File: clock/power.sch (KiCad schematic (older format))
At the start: 50 parts, among them Q501 BSS138, Q502 BSS138, U501 TPS56428, U502 TPS56428, U503 TPS56428

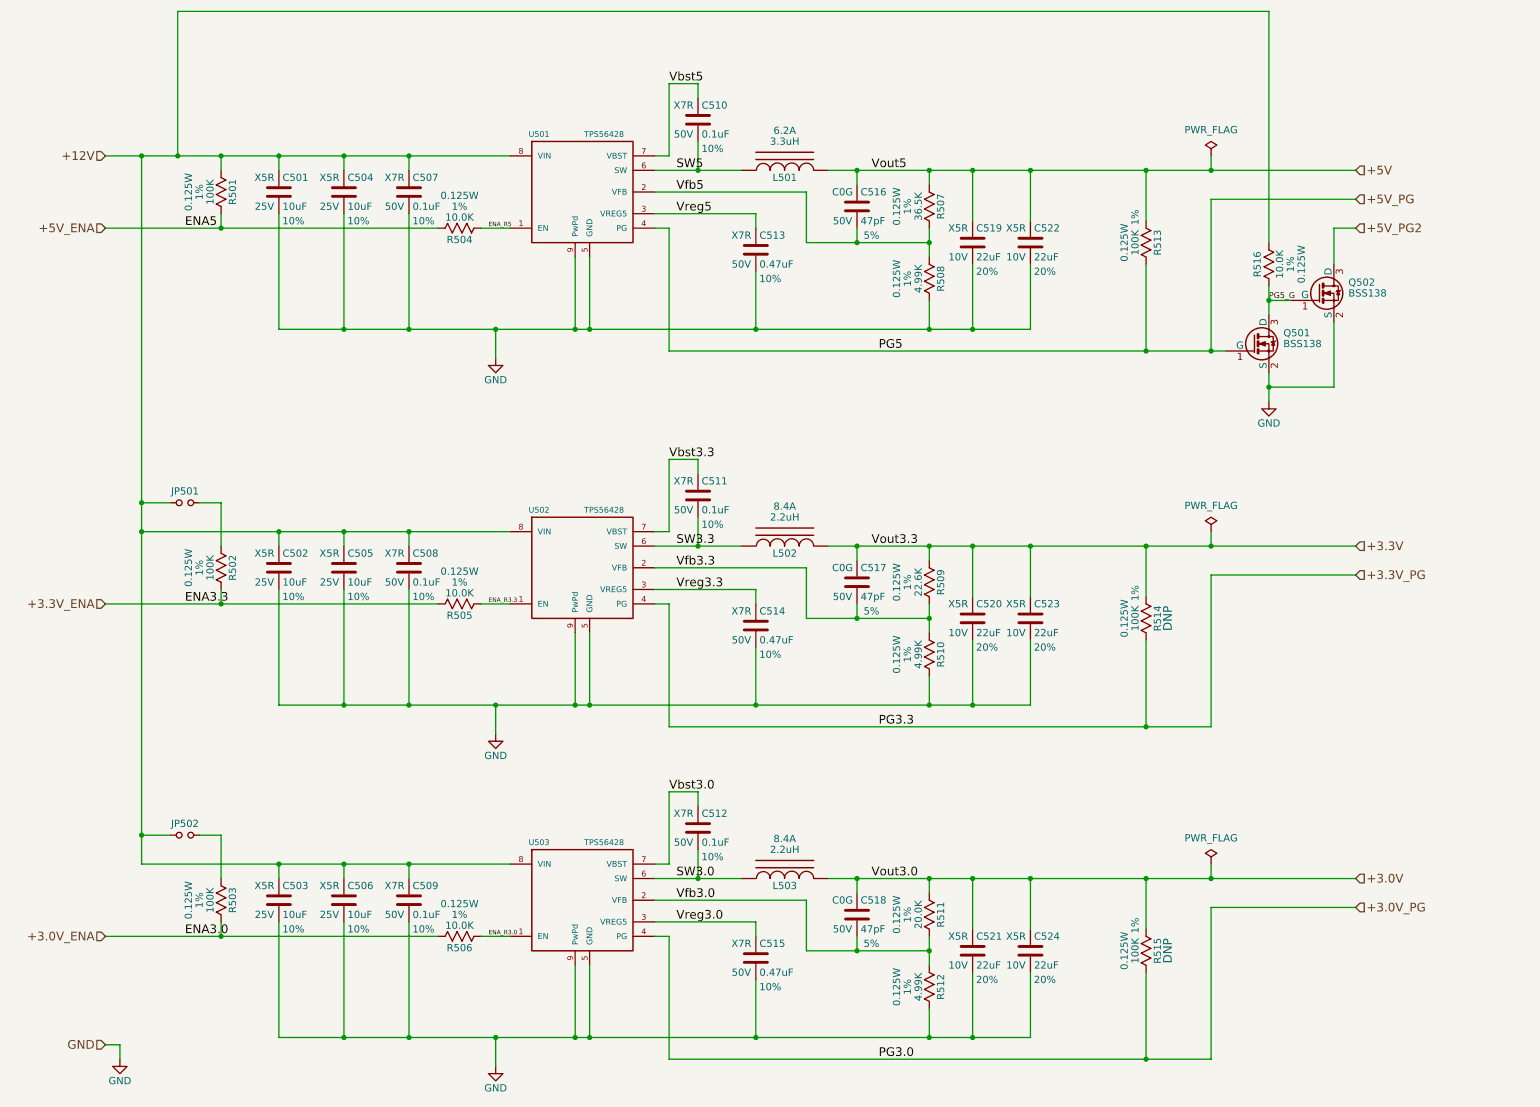
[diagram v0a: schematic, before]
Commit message: Start next revision of the main board. Power sequencing and control changes.
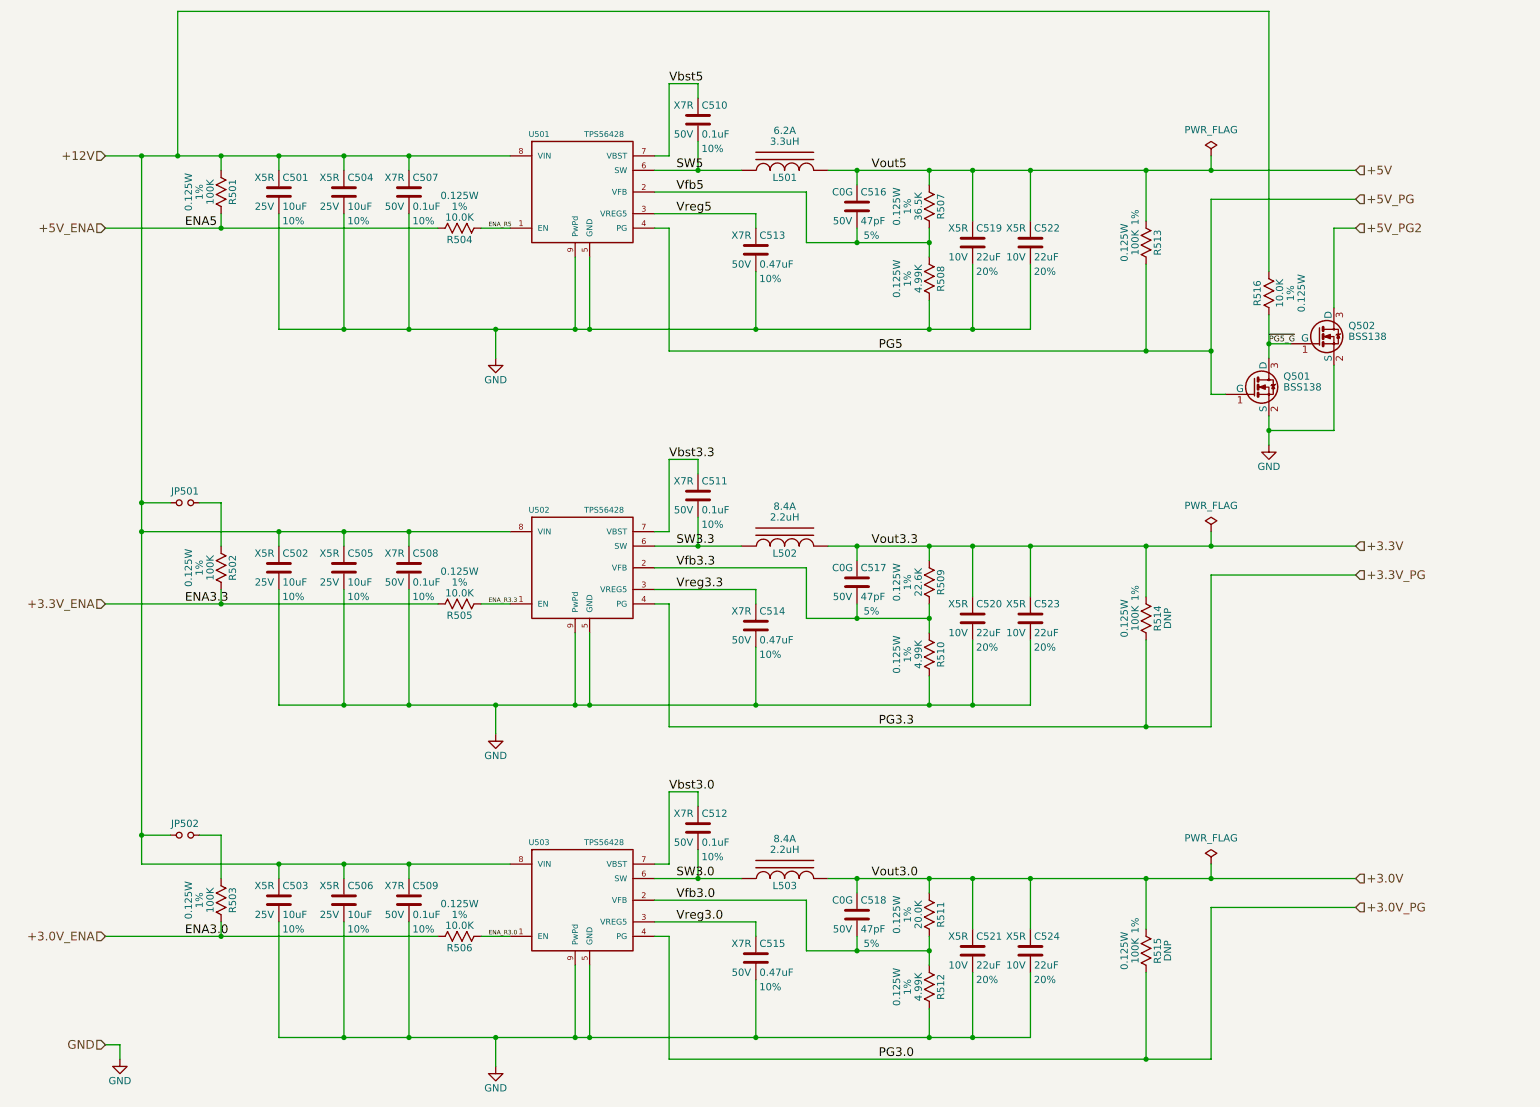
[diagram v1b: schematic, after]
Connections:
- net PG5_G renamed ~PG5_G~
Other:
- moved on the sheet: Q501, Q502, R516
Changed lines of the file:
@@
 	3500 2750 5800 2750
 Wire Wire Line
-	7400 3600 11250 3600
+	7400 3600 11150 3600
+Wire Wire Line
+	11150 2550 11150 3900
+Wire Wire Line
+	11150 3900 11250 3900
 Wire Wire Line
 	6850 3450 6850 2950
@@
 Connection ~ 4300 2750
 $Comp
-L GND #PWR072
+L GND #PWR075
 U 1 1 55FF67B4
 P 6200 3650
-F 0 "#PWR072" H 6200 3400 50  0001 C CNN
+F 0 "#PWR075" H 6200 3400 50  0001 C CNN
 F 1 "GND" H 6200 3500 50  0000 C CNN
 F 2 "" H 6200 3650 60  0000 C CNN
@@
 Connection ~ 4300 5350
 $Comp
-L GND #PWR073
+L GND #PWR076
 U 1 1 5619E4B9
 P 6200 6250
-F 0 "#PWR073" H 6200 6000 50  0001 C CNN
+F 0 "#PWR076" H 6200 6000 50  0001 C CNN
 F 1 "GND" H 6200 6100 50  0000 C CNN
 F 2 "" H 6200 6250 60  0000 C CNN
@@
 Connection ~ 4300 7650
 $Comp
-L GND #PWR074
+L GND #PWR077
 U 1 1 561A0FCA
 P 6200 8550
-F 0 "#PWR074" H 6200 8300 50  0001 C CNN
+F 0 "#PWR077" H 6200 8300 50  0001 C CNN
 F 1 "GND" H 6200 8400 50  0000 C CNN
 F 2 "" H 6200 8550 60  0000 C CNN
@@
 	12150 2550 11150 2550
 Wire Wire Line
-	11150 2550 11150 3600
-Wire Wire Line
 	12150 5150 11150 5150
 Wire Wire Line
@@
 F 6 "Vishay Dale" V 10700 5450 50  0001 C CNN "Manufacturer"
 F 7 "CRCW0805100KFKEA" V 10850 5450 50  0001 C CNN "PartNum"
-F 8 "DNP" V 10850 5450 60  0000 C CNN "DNP"
+F 8 "DNP" V 10850 5450 50  0000 C CNN "DNP"
 	1    10700 5450
 	1    0    0    -1
@@
 F 6 "Vishay Dale" V 10700 7750 50  0001 C CNN "Manufacturer"
 F 7 "CRCW0805100KFKEA" V 10850 7750 50  0001 C CNN "PartNum"
-F 8 "DNP" V 10850 7750 60  0000 C CNN "DNP"
+F 8 "DNP" V 10850 7750 50  0000 C CNN "DNP"
 	1    10700 7750
 	1    0    0    -1
@@
 GND
 $Comp
-L GND #PWR075
+L GND #PWR078
 U 1 1 563D8E93
 P 3600 8500
-F 0 "#PWR075" H 3600 8250 50  0001 C CNN
+F 0 "#PWR078" H 3600 8250 50  0001 C CNN
 F 1 "GND" H 3600 8350 50  0000 C CNN
 F 2 "" H 3600 8500 60  0000 C CNN
@@
 	3600 8400 3500 8400
 $Comp
-L PWR_FLAG #FLG076
+L PWR_FLAG #FLG079
 U 1 1 56439BF3
 P 11150 2250
-F 0 "#FLG076" H 11150 2345 50  0001 C CNN
+F 0 "#FLG079" H 11150 2345 50  0001 C CNN
 F 1 "PWR_FLAG" H 11150 2430 50  0000 C CNN
 F 2 "" H 11150 2250 60  0000 C CNN
@@
 Connection ~ 11150 2350
 $Comp
-L PWR_FLAG #FLG077
+L PWR_FLAG #FLG080
 U 1 1 5643A4B3
 P 11150 4850
-F 0 "#FLG077" H 11150 4945 50  0001 C CNN
+F 0 "#FLG080" H 11150 4945 50  0001 C CNN
 F 1 "PWR_FLAG" H 11150 5030 50  0000 C CNN
 F 2 "" H 11150 4850 60  0000 C CNN
@@
 Connection ~ 11150 4950
 $Comp
-L PWR_FLAG #FLG078
+L PWR_FLAG #FLG081
 U 1 1 5643AC28
 P 11150 7150
-F 0 "#FLG078" H 11150 7245 50  0001 C CNN
+F 0 "#FLG081" H 11150 7245 50  0001 C CNN
 F 1 "PWR_FLAG" H 11150 7330 50  0000 C CNN
 F 2 "" H 11150 7150 60  0000 C CNN
@@
 L BSS138 Q501
 U 1 1 57A96588
-P 11450 3550
-F 0 "Q501" H 11650 3625 50  0000 L CNN
-F 1 "BSS138" H 11650 3550 50  0000 L CNN
-F 2 "local:SOT-23-3_NXP_HandSoldering" H 11650 3475 50  0001 L CIN
-F 3 "" H 11450 3550 50  0000 L CNN
-F 4 "ON Semiconductor" H 11450 3550 60  0001 C CNN "Manufacturer"
-F 5 "BSS138LT1G" H 11450 3550 60  0001 C CNN "PartNum"
-	1    11450 3550
+P 11450 3850
+F 0 "Q501" H 11650 3925 50  0000 L CNN
+F 1 "BSS138" H 11650 3850 50  0000 L CNN
+F 2 "local:SOT-23-3_NXP_HandSoldering" H 11650 3775 50  0001 L CIN
+F 3 "" H 11450 3850 50  0000 L CNN
+F 4 "ON Semiconductor" H 11450 3850 60  0001 C CNN "Manufacturer"
+F 5 "BSS138LT1G" H 11450 3850 60  0001 C CNN "PartNum"
+	1    11450 3850
 	1    0    0    -1
 $EndComp
@@
 L BSS138 Q502
 U 1 1 57A97046
-P 11900 3200
-F 0 "Q502" H 12100 3275 50  0000 L CNN
-F 1 "BSS138" H 12100 3200 50  0000 L CNN
-F 2 "local:SOT-23-3_NXP_HandSoldering" H 12100 3125 50  0001 L CIN
-F 3 "" H 11900 3200 50  0000 L CNN
-F 4 "ON Semiconductor" H 11900 3200 60  0001 C CNN "Manufacturer"
-F 5 "BSS138LT1G" H 11900 3200 60  0001 C CNN "PartNum"
-	1    11900 3200
+P 11900 3500
+F 0 "Q502" H 12100 3575 50  0000 L CNN
+F 1 "BSS138" H 12100 3500 50  0000 L CNN
+F 2 "local:SOT-23-3_NXP_HandSoldering" H 12100 3425 50  0001 L CIN
+F 3 "" H 11900 3500 50  0000 L CNN
+F 4 "ON Semiconductor" H 11900 3500 60  0001 C CNN "Manufacturer"
+F 5 "BSS138LT1G" H 11900 3500 60  0001 C CNN "PartNum"
+	1    11900 3500
 	1    0    0    -1
 $EndComp
@@
 L R_local R516
 U 1 1 57A9749D
-P 11550 3000
-F 0 "R516" V 11630 3000 50  0000 C CNN
-F 1 "10.0K" V 11475 3000 50  0000 C CNN
-F 2 "Resistors_SMD:R_0805_HandSoldering" V 11480 3000 30  0001 C CNN
-F 3 "" V 11630 3000 30  0000 C CNN
-F 4 "1%" V 11400 3000 50  0000 C CNN "Tolerance"
-F 5 "0.125W" V 11325 3000 50  0000 C CNN "Power"
-F 6 "Vishay Dale" V 11550 3000 50  0001 C CNN "Manufacturer"
-F 7 "CRCW080510K0FKEA" V 11700 3000 50  0001 C CNN "PartNum"
-	1    11550 3000
+P 11550 3200
+F 0 "R516" V 11630 3200 50  0000 C CNN
+F 1 "10.0K" V 11475 3200 50  0000 C CNN
+F 2 "Resistors_SMD:R_0805_HandSoldering" V 11480 3200 30  0001 C CNN
+F 3 "" V 11630 3200 30  0000 C CNN
+F 4 "1%" V 11400 3200 50  0000 C CNN "Tolerance"
+F 5 "0.125W" V 11325 3200 50  0000 C CNN "Power"
+F 6 "Vishay Dale" V 11550 3200 50  0001 C CNN "Manufacturer"
+F 7 "CRCW080510K0FKEA" V 11700 3200 50  0001 C CNN "PartNum"
+	1    11550 3200
 	-1   0    0    1
 $EndComp
 Wire Wire Line
-	11550 3150 11550 3350
-Wire Wire Line
-	11700 3250 11550 3250
-Connection ~ 11550 3250
-Wire Wire Line
-	12000 3400 12000 3850
-Wire Wire Line
-	12000 3850 11550 3850
-Wire Wire Line
-	11550 3750 11550 3950
-$Comp
-L GND #PWR079
+	11550 3350 11550 3650
+Wire Wire Line
+	11700 3550 11550 3550
+Connection ~ 11550 3550
+Wire Wire Line
+	12000 3700 12000 4150
+Wire Wire Line
+	12000 4150 11550 4150
+Wire Wire Line
+	11550 4050 11550 4250
+$Comp
+L GND #PWR082
 U 1 1 57A97EAC
-P 11550 3950
-F 0 "#PWR079" H 11550 3700 50  0001 C CNN
-F 1 "GND" H 11550 3800 50  0000 C CNN
-F 2 "" H 11550 3950 60  0000 C CNN
-F 3 "" H 11550 3950 60  0000 C CNN
-	1    11550 3950
-	1    0    0    -1
-$EndComp
-Connection ~ 11550 3850
+P 11550 4250
+F 0 "#PWR082" H 11550 4000 50  0001 C CNN
+F 1 "GND" H 11550 4100 50  0000 C CNN
+F 2 "" H 11550 4250 60  0000 C CNN
+F 3 "" H 11550 4250 60  0000 C CNN
+	1    11550 4250
+	1    0    0    -1
+$EndComp
+Connection ~ 11550 4150
 Connection ~ 11150 3600
 Wire Wire Line
-	12000 3000 12000 2750
+	12000 3300 12000 2750
 Wire Wire Line
 	12000 2750 12150 2750
 Wire Wire Line
-	11550 2850 11550 1250
+	11550 3050 11550 1250
 Wire Wire Line
 	11550 1250 4000 1250
@@
 	4000 1250 4000 2250
 Connection ~ 4000 2250
-Text Label 11550 3250 0    40   ~ 0
-PG5_G
+Text Label 11550 3550 0    40   ~ 0
+~PG5_G~
 $EndSCHEMATC

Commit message: Checkpoint layout. Update hand soldering footprints for 0805 parts.
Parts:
- C507, C508, C509, C510, C511, C512, C513, C514, C515, C516, C517, C518: footprint Capacitors_SMD:C_0805_HandSoldering -> local:C_0805_HandSoldering
- R501, R502, R503, R504, R505, R506, R507, R508, R509, R510, R511, R512, R513, R514, R515, R516: footprint Resistors_SMD:R_0805_HandSoldering -> local:R_0805_HandSoldering
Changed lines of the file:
@@
 F 0 "C507" H 5625 2600 50  0000 L CNN
 F 1 "0.1uF" H 5625 2400 50  0000 L CNN
-F 2 "Capacitors_SMD:C_0805_HandSoldering" H 5638 2350 30  0001 C CNN
+F 2 "local:C_0805_HandSoldering" H 5638 2350 30  0001 C CNN
 F 3 "" H 5600 2500 60  0000 C CNN
 F 4 "50V" H 5500 2400 50  0000 C CNN "Voltage"
@@
 F 0 "R501" V 4380 2500 50  0000 C CNN
 F 1 "100K" V 4225 2500 50  0000 C CNN
-F 2 "Resistors_SMD:R_0805_HandSoldering" V 4230 2500 30  0001 C CNN
+F 2 "local:R_0805_HandSoldering" V 4230 2500 30  0001 C CNN
 F 3 "" V 4380 2500 30  0000 C CNN
 F 4 "1%" V 4150 2500 50  0000 C CNN "Tolerance"
@@
 F 0 "R504" V 6030 2750 50  0000 C CNN
 F 1 "10.0K" V 5875 2750 50  0000 C CNN
-F 2 "Resistors_SMD:R_0805_HandSoldering" V 5880 2750 30  0001 C CNN
+F 2 "local:R_0805_HandSoldering" V 5880 2750 30  0001 C CNN
 F 3 "" V 6030 2750 30  0000 C CNN
 F 4 "1%" V 5800 2750 50  0000 C CNN "Tolerance"
@@
 F 0 "R513" V 10780 2850 50  0000 C CNN
 F 1 "100K" V 10625 2850 50  0000 C CNN
-F 2 "Resistors_SMD:R_0805_HandSoldering" V 10630 2850 30  0001 C CNN
+F 2 "local:R_0805_HandSoldering" V 10630 2850 30  0001 C CNN
 F 3 "" V 10780 2850 30  0000 C CNN
 F 4 "1%" V 10625 3025 50  0000 C CNN "Tolerance"
@@
 F 0 "C510" H 7625 2100 50  0000 L CNN
 F 1 "0.1uF" H 7625 1900 50  0000 L CNN
-F 2 "Capacitors_SMD:C_0805_HandSoldering" H 7638 1850 30  0001 C CNN
+F 2 "local:C_0805_HandSoldering" H 7638 1850 30  0001 C CNN
 F 3 "" H 7600 2000 60  0000 C CNN
 F 4 "50V" H 7500 1900 50  0000 C CNN "Voltage"
@@
 F 0 "C513" H 8025 3000 50  0000 L CNN
 F 1 "0.47uF" H 8025 2800 50  0000 L CNN
-F 2 "Capacitors_SMD:C_0805_HandSoldering" H 8038 2750 30  0001 C CNN
+F 2 "local:C_0805_HandSoldering" H 8038 2750 30  0001 C CNN
 F 3 "" H 8000 2900 60  0000 C CNN
 F 4 "50V" H 7900 2800 50  0000 C CNN "Voltage"
@@
 F 0 "C508" H 5625 5200 50  0000 L CNN
 F 1 "0.1uF" H 5625 5000 50  0000 L CNN
-F 2 "Capacitors_SMD:C_0805_HandSoldering" H 5638 4950 30  0001 C CNN
+F 2 "local:C_0805_HandSoldering" H 5638 4950 30  0001 C CNN
 F 3 "" H 5600 5100 60  0000 C CNN
 F 4 "50V" H 5500 5000 50  0000 C CNN "Voltage"
@@
 F 0 "R505" V 6030 5350 50  0000 C CNN
 F 1 "10.0K" V 5875 5350 50  0000 C CNN
-F 2 "Resistors_SMD:R_0805_HandSoldering" V 5880 5350 30  0001 C CNN
+F 2 "local:R_0805_HandSoldering" V 5880 5350 30  0001 C CNN
 F 3 "" V 6030 5350 30  0000 C CNN
 F 4 "1%" V 5800 5350 50  0000 C CNN "Tolerance"
@@
 F 0 "R502" V 4380 5100 50  0000 C CNN
 F 1 "100K" V 4225 5100 50  0000 C CNN
-F 2 "Resistors_SMD:R_0805_HandSoldering" V 4230 5100 30  0001 C CNN
+F 2 "local:R_0805_HandSoldering" V 4230 5100 30  0001 C CNN
 F 3 "" V 4380 5100 30  0000 C CNN
 F 4 "1%" V 4150 5100 50  0000 C CNN "Tolerance"
@@
 F 0 "C511" H 7625 4700 50  0000 L CNN
 F 1 "0.1uF" H 7625 4500 50  0000 L CNN
-F 2 "Capacitors_SMD:C_0805_HandSoldering" H 7638 4450 30  0001 C CNN
+F 2 "local:C_0805_HandSoldering" H 7638 4450 30  0001 C CNN
 F 3 "" H 7600 4600 60  0000 C CNN
 F 4 "50V" H 7500 4500 50  0000 C CNN "Voltage"
@@
 F 0 "C514" H 8025 5600 50  0000 L CNN
 F 1 "0.47uF" H 8025 5400 50  0000 L CNN
-F 2 "Capacitors_SMD:C_0805_HandSoldering" H 8038 5350 30  0001 C CNN
+F 2 "local:C_0805_HandSoldering" H 8038 5350 30  0001 C CNN
 F 3 "" H 8000 5500 60  0000 C CNN
 F 4 "50V" H 7900 5400 50  0000 C CNN "Voltage"
@@
 F 0 "R514" V 10780 5450 50  0000 C CNN
 F 1 "100K" V 10625 5450 50  0000 C CNN
-F 2 "Resistors_SMD:R_0805_HandSoldering" V 10630 5450 30  0001 C CNN
+F 2 "local:R_0805_HandSoldering" V 10630 5450 30  0001 C CNN
 F 3 "" V 10780 5450 30  0000 C CNN
 F 4 "1%" V 10625 5625 50  0000 C CNN "Tolerance"
@@
 F 0 "R515" V 10780 7750 50  0000 C CNN
 F 1 "100K" V 10625 7750 50  0000 C CNN
-F 2 "Resistors_SMD:R_0805_HandSoldering" V 10630 7750 30  0001 C CNN
+F 2 "local:R_0805_HandSoldering" V 10630 7750 30  0001 C CNN
 F 3 "" V 10780 7750 30  0000 C CNN
 F 4 "1%" V 10625 7925 50  0000 C CNN "Tolerance"
@@
 F 0 "C515" H 8025 7900 50  0000 L CNN
 F 1 "0.47uF" H 8025 7700 50  0000 L CNN
-F 2 "Capacitors_SMD:C_0805_HandSoldering" H 8038 7650 30  0001 C CNN
+F 2 "local:C_0805_HandSoldering" H 8038 7650 30  0001 C CNN
 F 3 "" H 8000 7800 60  0000 C CNN
 F 4 "50V" H 7900 7700 50  0000 C CNN "Voltage"
@@
 F 0 "C512" H 7625 7000 50  0000 L CNN
 F 1 "0.1uF" H 7625 6800 50  0000 L CNN
-F 2 "Capacitors_SMD:C_0805_HandSoldering" H 7638 6750 30  0001 C CNN
+F 2 "local:C_0805_HandSoldering" H 7638 6750 30  0001 C CNN
 F 3 "" H 7600 6900 60  0000 C CNN
 F 4 "50V" H 7500 6800 50  0000 C CNN "Voltage"
@@
 F 0 "R506" V 6030 7650 50  0000 C CNN
 F 1 "10.0K" V 5875 7650 50  0000 C CNN
-F 2 "Resistors_SMD:R_0805_HandSoldering" V 5880 7650 30  0001 C CNN
+F 2 "local:R_0805_HandSoldering" V 5880 7650 30  0001 C CNN
 F 3 "" V 6030 7650 30  0000 C CNN
 F 4 "1%" V 5800 7650 50  0000 C CNN "Tolerance"
@@
 F 0 "C509" H 5625 7500 50  0000 L CNN
 F 1 "0.1uF" H 5625 7300 50  0000 L CNN
-F 2 "Capacitors_SMD:C_0805_HandSoldering" H 5638 7250 30  0001 C CNN
+F 2 "local:C_0805_HandSoldering" H 5638 7250 30  0001 C CNN
 F 3 "" H 5600 7400 60  0000 C CNN
 F 4 "50V" H 5500 7300 50  0000 C CNN "Voltage"
@@
 F 0 "R503" V 4380 7400 50  0000 C CNN
 F 1 "100K" V 4225 7400 50  0000 C CNN
-F 2 "Resistors_SMD:R_0805_HandSoldering" V 4230 7400 30  0001 C CNN
+F 2 "local:R_0805_HandSoldering" V 4230 7400 30  0001 C CNN
 F 3 "" V 4380 7400 30  0000 C CNN
 F 4 "1%" V 4150 7400 50  0000 C CNN "Tolerance"
@@
 F 0 "R508" V 9280 3100 50  0000 C CNN
 F 1 "4.99K" V 9125 3100 50  0000 C CNN
-F 2 "Resistors_SMD:R_0805_HandSoldering" V 9130 3100 30  0001 C CNN
+F 2 "local:R_0805_HandSoldering" V 9130 3100 30  0001 C CNN
 F 3 "" V 9280 3100 30  0000 C CNN
 F 4 "1%" V 9050 3100 50  0000 C CNN "Tolerance"
@@
 F 0 "R507" V 9280 2600 50  0000 C CNN
 F 1 "36.5K" V 9125 2600 50  0000 C CNN
-F 2 "Resistors_SMD:R_0805_HandSoldering" V 9130 2600 30  0001 C CNN
+F 2 "local:R_0805_HandSoldering" V 9130 2600 30  0001 C CNN
 F 3 "" V 9280 2600 30  0000 C CNN
 F 4 "1%" V 9050 2600 50  0000 C CNN "Tolerance"
@@
 F 0 "R510" V 9280 5700 50  0000 C CNN
 F 1 "4.99K" V 9125 5700 50  0000 C CNN
-F 2 "Resistors_SMD:R_0805_HandSoldering" V 9130 5700 30  0001 C CNN
+F 2 "local:R_0805_HandSoldering" V 9130 5700 30  0001 C CNN
 F 3 "" V 9280 5700 30  0000 C CNN
 F 4 "1%" V 9050 5700 50  0000 C CNN "Tolerance"
@@
 F 0 "R512" V 9280 8000 50  0000 C CNN
 F 1 "4.99K" V 9125 8000 50  0000 C CNN
-F 2 "Resistors_SMD:R_0805_HandSoldering" V 9130 8000 30  0001 C CNN
+F 2 "local:R_0805_HandSoldering" V 9130 8000 30  0001 C CNN
 F 3 "" V 9280 8000 30  0000 C CNN
 F 4 "1%" V 9050 8000 50  0000 C CNN "Tolerance"
@@
 F 0 "R509" V 9280 5200 50  0000 C CNN
 F 1 "22.6K" V 9125 5200 50  0000 C CNN
-F 2 "Resistors_SMD:R_0805_HandSoldering" V 9130 5200 30  0001 C CNN
+F 2 "local:R_0805_HandSoldering" V 9130 5200 30  0001 C CNN
 F 3 "" V 9280 5200 30  0000 C CNN
 F 4 "1%" V 9050 5200 50  0000 C CNN "Tolerance"
@@
 F 0 "R511" V 9280 7500 50  0000 C CNN
 F 1 "20.0K" V 9125 7500 50  0000 C CNN
-F 2 "Resistors_SMD:R_0805_HandSoldering" V 9130 7500 30  0001 C CNN
+F 2 "local:R_0805_HandSoldering" V 9130 7500 30  0001 C CNN
 F 3 "" V 9280 7500 30  0000 C CNN
 F 4 "1%" V 9050 7500 50  0000 C CNN "Tolerance"
@@
 F 0 "C516" H 8725 2700 50  0000 L CNN
 F 1 "47pF" H 8725 2500 50  0000 L CNN
-F 2 "Capacitors_SMD:C_0805_HandSoldering" H 8738 2450 30  0001 C CNN
+F 2 "local:C_0805_HandSoldering" H 8738 2450 30  0001 C CNN
 F 3 "" H 8700 2600 60  0000 C CNN
 F 4 "50V" H 8600 2500 50  0000 C CNN "Voltage"
@@
 F 0 "C517" H 8725 5300 50  0000 L CNN
 F 1 "47pF" H 8725 5100 50  0000 L CNN
-F 2 "Capacitors_SMD:C_0805_HandSoldering" H 8738 5050 30  0001 C CNN
+F 2 "local:C_0805_HandSoldering" H 8738 5050 30  0001 C CNN
 F 3 "" H 8700 5200 60  0000 C CNN
 F 4 "50V" H 8600 5100 50  0000 C CNN "Voltage"
@@
 F 0 "C518" H 8725 7600 50  0000 L CNN
 F 1 "47pF" H 8725 7400 50  0000 L CNN
-F 2 "Capacitors_SMD:C_0805_HandSoldering" H 8738 7350 30  0001 C CNN
+F 2 "local:C_0805_HandSoldering" H 8738 7350 30  0001 C CNN
 F 3 "" H 8700 7500 60  0000 C CNN
 F 4 "50V" H 8600 7400 50  0000 C CNN "Voltage"
@@
 F 0 "R516" V 11630 3200 50  0000 C CNN
 F 1 "10.0K" V 11475 3200 50  0000 C CNN
-F 2 "Resistors_SMD:R_0805_HandSoldering" V 11480 3200 30  0001 C CNN
+F 2 "local:R_0805_HandSoldering" V 11480 3200 30  0001 C CNN
 F 3 "" V 11630 3200 30  0000 C CNN
 F 4 "1%" V 11400 3200 50  0000 C CNN "Tolerance"
